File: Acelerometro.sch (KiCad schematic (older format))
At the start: 9 parts, among them Q6 BSS138, Q7 BSS138, U8 MMA7660FC

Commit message: version preliminar de la etapa de alimentacion
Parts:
- renumbered C13 to C12, C14 to C13, Q6 to Q3, Q7 to Q4, R32 to R12, R33 to R13, R34 to R14, R35 to R15, U8 to U5
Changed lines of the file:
@@
 LIBS:Sensores
 LIBS:Reles
+LIBS:Reguladores
+LIBS:Transistores
 LIBS:Wifi_PB-cache
 EELAYER 26 0
@@
 $Descr User 8268 5846
 encoding utf-8
-Sheet 4 11
+Sheet 4 15
 Title "Acelerometro 3 ejes"
 Date "2017-01-15"
@@
 $EndDescr
 $Comp
-L BSS138 Q6
+L BSS138 Q3
 U 1 1 57952913
 P 5250 2100
-F 0 "Q6" V 5486 2100 50  0000 C CNN
+F 0 "Q3" V 5486 2100 50  0000 C CNN
 F 1 "BSS138" V 5577 2100 50  0000 C CNN
 F 2 "TO_SOT_Packages_SMD:SOT-23" H 5450 2025 50  0001 L CIN
@@
 $EndComp
 $Comp
-L +3V3 #PWR065
+L +3V3 #PWR28
 U 1 1 57952AC0
 P 5200 1450
-F 0 "#PWR065" H 5200 1300 50  0001 C CNN
+F 0 "#PWR28" H 5200 1300 50  0001 C CNN
 F 1 "+3V3" H 5215 1623 50  0000 C CNN
 F 2 "" H 5200 1450 50  0000 C CNN
@@
 $EndComp
 $Comp
-L R R32
+L R R12
 U 1 1 57952AE0
 P 4150 1900
-F 0 "R32" H 4220 1946 50  0000 L CNN
+F 0 "R12" H 4220 1946 50  0000 L CNN
 F 1 "4K7" H 4220 1855 50  0000 L CNN
 F 2 "Resistencias:R_0805" V 4080 1900 50  0001 C CNN
@@
 SCL2
 $Comp
-L BSS138 Q7
+L BSS138 Q4
 U 1 1 57952D65
 P 5900 2600
-F 0 "Q7" V 6136 2600 50  0000 C CNN
+F 0 "Q4" V 6136 2600 50  0000 C CNN
 F 1 "BSS138" V 6227 2600 50  0000 C CNN
 F 2 "TO_SOT_Packages_SMD:SOT-23" H 6100 2525 50  0001 L CIN
@@
 $EndComp
 $Comp
-L +5V #PWR066
+L +5V #PWR29
 U 1 1 57952EB0
 P 6200 1450
-F 0 "#PWR066" H 6200 1300 50  0001 C CNN
+F 0 "#PWR29" H 6200 1300 50  0001 C CNN
 F 1 "+5V" H 6215 1623 50  0000 C CNN
 F 2 "" H 6200 1450 50  0000 C CNN
@@
 $EndComp
 $Comp
-L +5V #PWR067
+L +5V #PWR30
 U 1 1 57952EEB
 P 6500 1450
-F 0 "#PWR067" H 6500 1300 50  0001 C CNN
+F 0 "#PWR30" H 6500 1300 50  0001 C CNN
 F 1 "+5V" H 6515 1623 50  0000 C CNN
 F 2 "" H 6500 1450 50  0000 C CNN
@@
 $EndComp
 $Comp
-L MMA7660FC U8
+L MMA7660FC U5
 U 1 1 57953056
 P 2650 2400
-F 0 "U8" H 2650 3077 100 0000 C CNN
+F 0 "U5" H 2650 3077 100 0000 C CNN
 F 1 "MMA7660FC" H 2650 2911 100 0000 C CNN
 F 2 "Housings_DFN_QFN:DFN-10-1EP_3x3mm_Pitch0.5mm" H 2500 2400 100 0001 C CNN
@@
 $EndComp
 $Comp
-L GND #PWR068
+L GND #PWR27
 U 1 1 579532CA
 P 3550 3050
-F 0 "#PWR068" H 3550 2800 50  0001 C CNN
+F 0 "#PWR27" H 3550 2800 50  0001 C CNN
 F 1 "GND" H 3555 2877 50  0000 C CNN
 F 2 "" H 3550 3050 50  0000 C CNN
@@
 $EndComp
 $Comp
-L GND #PWR069
+L GND #PWR20
 U 1 1 5795333D
 P 1500 3050
-F 0 "#PWR069" H 1500 2800 50  0001 C CNN
+F 0 "#PWR20" H 1500 2800 50  0001 C CNN
 F 1 "GND" H 1505 2877 50  0000 C CNN
 F 2 "" H 1500 3050 50  0000 C CNN
@@
 $EndComp
 $Comp
-L +3V3 #PWR070
+L +3V3 #PWR21
 U 1 1 579533C4
 P 1900 1650
-F 0 "#PWR070" H 1900 1500 50  0001 C CNN
+F 0 "#PWR21" H 1900 1500 50  0001 C CNN
 F 1 "+3V3" H 1915 1823 50  0000 C CNN
 F 2 "" H 1900 1650 50  0000 C CNN
@@
 $EndComp
 $Comp
-L +3V3 #PWR071
+L +3V3 #PWR26
 U 1 1 57953474
 P 3400 1650
-F 0 "#PWR071" H 3400 1500 50  0001 C CNN
+F 0 "#PWR26" H 3400 1500 50  0001 C CNN
 F 1 "+3V3" H 3415 1823 50  0000 C CNN
 F 2 "" H 3400 1650 50  0000 C CNN
@@
 $EndComp
 $Comp
-L R R33
+L R R13
 U 1 1 57953886
 P 4500 1900
-F 0 "R33" H 4570 1946 50  0000 L CNN
+F 0 "R13" H 4570 1946 50  0000 L CNN
 F 1 "4K7" H 4570 1855 50  0000 L CNN
 F 2 "Resistencias:R_0805" V 4430 1900 50  0001 C CNN
@@
 $EndComp
 $Comp
-L R R34
+L R R14
 U 1 1 579538BB
 P 6200 1850
-F 0 "R34" H 6270 1896 50  0000 L CNN
+F 0 "R14" H 6270 1896 50  0000 L CNN
 F 1 "4K7" H 6270 1805 50  0000 L CNN
 F 2 "Resistencias:R_0805" V 6130 1850 50  0001 C CNN
@@
 $EndComp
 $Comp
-L R R35
+L R R15
 U 1 1 57953937
 P 6500 1850
-F 0 "R35" H 6570 1896 50  0000 L CNN
+F 0 "R15" H 6570 1896 50  0000 L CNN
 F 1 "4K7" H 6570 1805 50  0000 L CNN
 F 2 "Resistencias:R_0805" V 6430 1850 50  0001 C CNN
@@
 $EndComp
 $Comp
-L C C13
+L C C12
 U 1 1 57953EAD
 P 2150 3650
-F 0 "C13" H 2175 3750 50  0000 L CNN
+F 0 "C12" H 2175 3750 50  0000 L CNN
 F 1 "100n" H 2175 3550 50  0000 L CNN
 F 2 "Capacitors_SMD:C_0805" H 2188 3500 50  0001 C CNN
@@
 $EndComp
 $Comp
-L GND #PWR072
+L GND #PWR23
 U 1 1 57953EB4
 P 2150 3900
-F 0 "#PWR072" H 2150 3650 50  0001 C CNN
+F 0 "#PWR23" H 2150 3650 50  0001 C CNN
 F 1 "GND" H 2150 3750 50  0000 C CNN
 F 2 "" H 2150 3900 50  0000 C CNN
@@
 $EndComp
 $Comp
-L C C14
+L C C13
 U 1 1 57953F77
 P 3100 3650
-F 0 "C14" H 3125 3750 50  0000 L CNN
+F 0 "C13" H 3125 3750 50  0000 L CNN
 F 1 "100n" H 3125 3550 50  0000 L CNN
 F 2 "Capacitors_SMD:C_0805" H 3138 3500 50  0001 C CNN
@@
 $EndComp
 $Comp
-L GND #PWR073
+L GND #PWR25
 U 1 1 57953F7E
 P 3100 3900
-F 0 "#PWR073" H 3100 3650 50  0001 C CNN
+F 0 "#PWR25" H 3100 3650 50  0001 C CNN
 F 1 "GND" H 3100 3750 50  0000 C CNN
 F 2 "" H 3100 3900 50  0000 C CNN
@@
 $EndComp
 $Comp
-L +3V3 #PWR074
+L +3V3 #PWR22
 U 1 1 57953FC4
 P 2150 3350
-F 0 "#PWR074" H 2150 3200 50  0001 C CNN
+F 0 "#PWR22" H 2150 3200 50  0001 C CNN
 F 1 "+3V3" H 2165 3523 50  0000 C CNN
 F 2 "" H 2150 3350 50  0000 C CNN
@@
 $EndComp
 $Comp
-L +3V3 #PWR075
+L +3V3 #PWR24
 U 1 1 57954005
 P 3100 3350
-F 0 "#PWR075" H 3100 3200 50  0001 C CNN
+F 0 "#PWR24" H 3100 3200 50  0001 C CNN
 F 1 "+3V3" H 3115 3523 50  0000 C CNN
 F 2 "" H 3100 3350 50  0000 C CNN

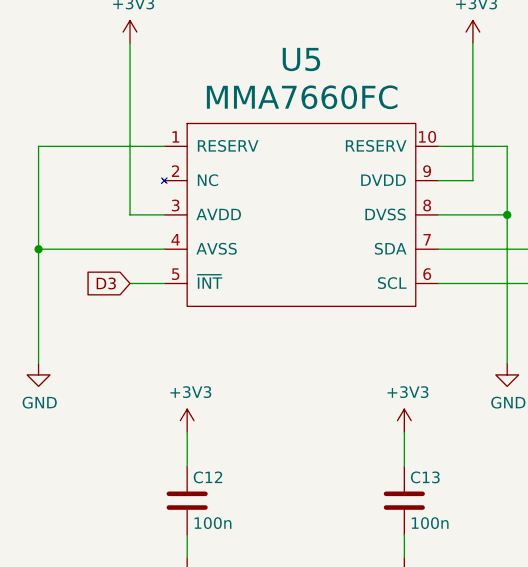
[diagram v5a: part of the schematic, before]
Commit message: conectar reset gpio. retocar plano masa
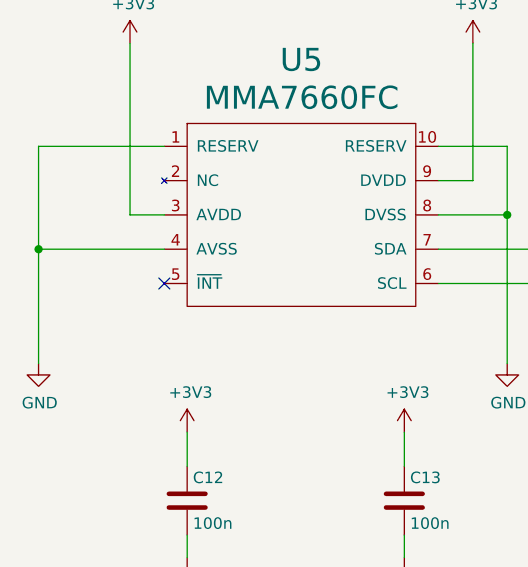
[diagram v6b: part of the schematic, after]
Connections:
- net D3: no longer names the net of U5.5 (~INT)
- no-connect marks 0 -> 1
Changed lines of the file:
@@
 $EndComp
 $Comp
-L +3V3 #PWR040
+L +3V3 #PWR041
 U 1 1 57952AC0
 P 5200 1450
-F 0 "#PWR040" H 5200 1300 50  0001 C CNN
+F 0 "#PWR041" H 5200 1300 50  0001 C CNN
 F 1 "+3V3" H 5215 1623 50  0000 C CNN
 F 2 "" H 5200 1450 50  0000 C CNN
@@
 $EndComp
 $Comp
-L +5V #PWR041
+L +5V #PWR042
 U 1 1 57952EB0
 P 6200 1450
-F 0 "#PWR041" H 6200 1300 50  0001 C CNN
+F 0 "#PWR042" H 6200 1300 50  0001 C CNN
 F 1 "+5V" H 6215 1623 50  0000 C CNN
 F 2 "" H 6200 1450 50  0000 C CNN
@@
 $EndComp
 $Comp
-L +5V #PWR042
+L +5V #PWR043
 U 1 1 57952EEB
 P 6500 1450
-F 0 "#PWR042" H 6500 1300 50  0001 C CNN
+F 0 "#PWR043" H 6500 1300 50  0001 C CNN
 F 1 "+5V" H 6515 1623 50  0000 C CNN
 F 2 "" H 6500 1450 50  0000 C CNN
@@
 $EndComp
 $Comp
-L GND #PWR043
+L GND #PWR044
 U 1 1 579532CA
 P 3550 3050
-F 0 "#PWR043" H 3550 2800 50  0001 C CNN
+F 0 "#PWR044" H 3550 2800 50  0001 C CNN
 F 1 "GND" H 3555 2877 50  0000 C CNN
 F 2 "" H 3550 3050 50  0000 C CNN
@@
 $EndComp
 $Comp
-L GND #PWR044
+L GND #PWR045
 U 1 1 5795333D
 P 1500 3050
-F 0 "#PWR044" H 1500 2800 50  0001 C CNN
+F 0 "#PWR045" H 1500 2800 50  0001 C CNN
 F 1 "GND" H 1505 2877 50  0000 C CNN
 F 2 "" H 1500 3050 50  0000 C CNN
@@
 $EndComp
 $Comp
-L +3V3 #PWR045
+L +3V3 #PWR046
 U 1 1 579533C4
 P 1900 1650
-F 0 "#PWR045" H 1900 1500 50  0001 C CNN
+F 0 "#PWR046" H 1900 1500 50  0001 C CNN
 F 1 "+3V3" H 1915 1823 50  0000 C CNN
 F 2 "" H 1900 1650 50  0000 C CNN
@@
 $EndComp
 $Comp
-L +3V3 #PWR046
+L +3V3 #PWR047
 U 1 1 57953474
 P 3400 1650
-F 0 "#PWR046" H 3400 1500 50  0001 C CNN
+F 0 "#PWR047" H 3400 1500 50  0001 C CNN
 F 1 "+3V3" H 3415 1823 50  0000 C CNN
 F 2 "" H 3400 1650 50  0000 C CNN
@@
 $EndComp
 $Comp
-L GND #PWR047
+L GND #PWR048
 U 1 1 57953EB4
 P 2150 3900
-F 0 "#PWR047" H 2150 3650 50  0001 C CNN
+F 0 "#PWR048" H 2150 3650 50  0001 C CNN
 F 1 "GND" H 2150 3750 50  0000 C CNN
 F 2 "" H 2150 3900 50  0000 C CNN
@@
 $EndComp
 $Comp
-L GND #PWR048
+L GND #PWR049
 U 1 1 57953F7E
 P 3100 3900
-F 0 "#PWR048" H 3100 3650 50  0001 C CNN
+F 0 "#PWR049" H 3100 3650 50  0001 C CNN
 F 1 "GND" H 3100 3750 50  0000 C CNN
 F 2 "" H 3100 3900 50  0000 C CNN
@@
 $EndComp
 $Comp
-L +3V3 #PWR049
+L +3V3 #PWR050
 U 1 1 57953FC4
 P 2150 3350
-F 0 "#PWR049" H 2150 3200 50  0001 C CNN
+F 0 "#PWR050" H 2150 3200 50  0001 C CNN
 F 1 "+3V3" H 2165 3523 50  0000 C CNN
 F 2 "" H 2150 3350 50  0000 C CNN
@@
 $EndComp
 $Comp
-L +3V3 #PWR050
+L +3V3 #PWR051
 U 1 1 57954005
 P 3100 3350
-F 0 "#PWR050" H 3100 3200 50  0001 C CNN
+F 0 "#PWR051" H 3100 3200 50  0001 C CNN
 F 1 "+3V3" H 3115 3523 50  0000 C CNN
 F 2 "" H 3100 3350 50  0000 C CNN
@@
 $Bitmap
 Pos 7500 4400
-Scale 0,350000
+Scale 0,000000
 Data
 89 50 4E 47 0D 0A 1A 0A 00 00 00 0D 49 48 44 52 00 00 01 D5 00 00 01 ED 08 06 00 00 00 4F 90 E4
@@
 EndData
 $EndBitmap
-Text GLabel 1900 2700 0    50   Input ~ 0
-D3
 Text GLabel 4150 3000 3    60   BiDi ~ 0
 SDA
@@
 Wire Wire Line
 	3100 3900 3100 3800
-Wire Wire Line
-	2050 2700 1900 2700
+NoConn ~ 2050 2700
 $EndSCHEMATC
